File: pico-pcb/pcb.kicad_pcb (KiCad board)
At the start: 2 copper layers, 53.3 x 71.1 mm, 28 parts, among them J1 AudioJack1, J2 AudioJack2, Q1 2N3904, SW1 SW_DIP_x04, U1 Pico

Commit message: Updated PCB .50mm traces now and rewired trrs jack to match digirig type cabling.
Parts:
-  : renamed from REF** (x2)
- 3.2mm M3: renamed from REF** (x2)
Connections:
- J1 pad R1: SP -> MIC
- J1 pad T: MIC -> SP
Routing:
- net GND: track 204.5 -> 199.8 mm
- net PTT_R: track 146.2 -> 143.3 mm
- net MIC: track 16.0 -> 17.7 mm
- net SP: track 11.9 -> 11.0 mm

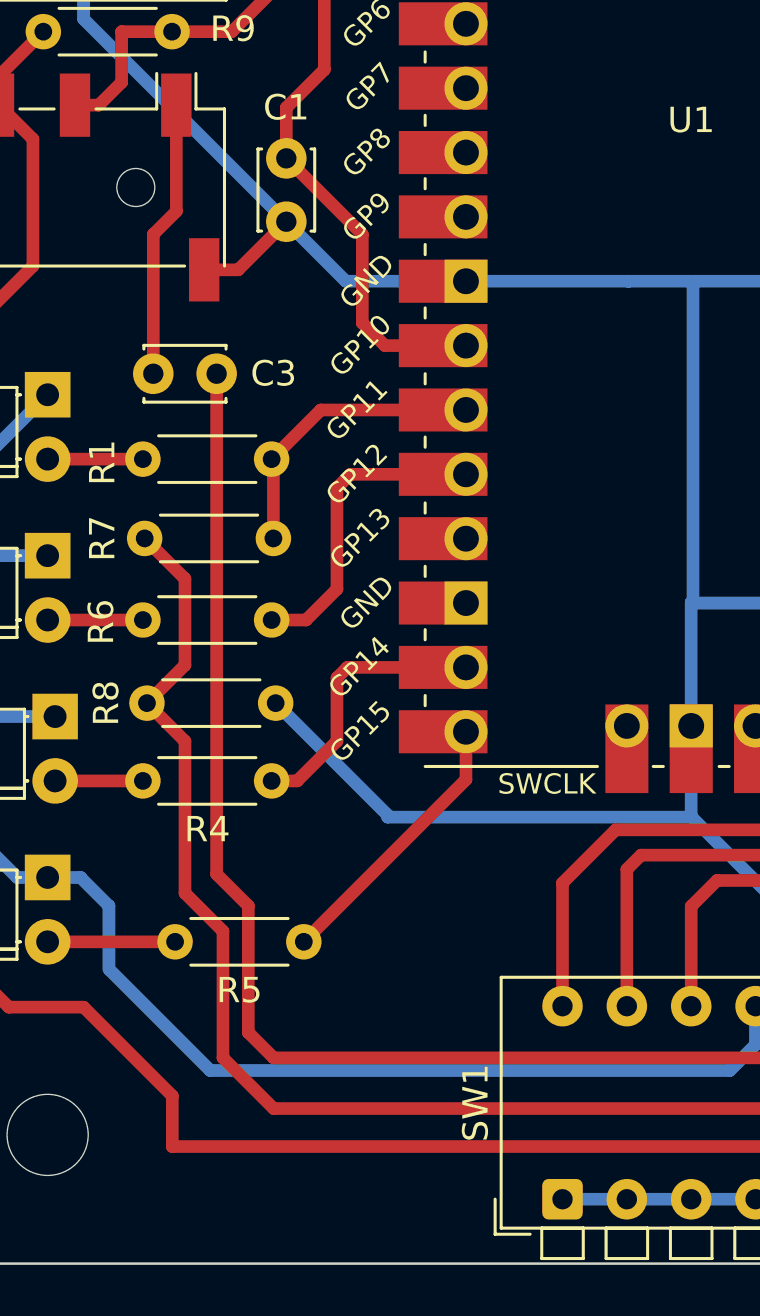
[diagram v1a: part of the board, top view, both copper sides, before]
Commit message: Updated Schematic and PCB to add 100ohm resistor to pwm circuit as per original pico tnc and recommendation by Mario AE0GL
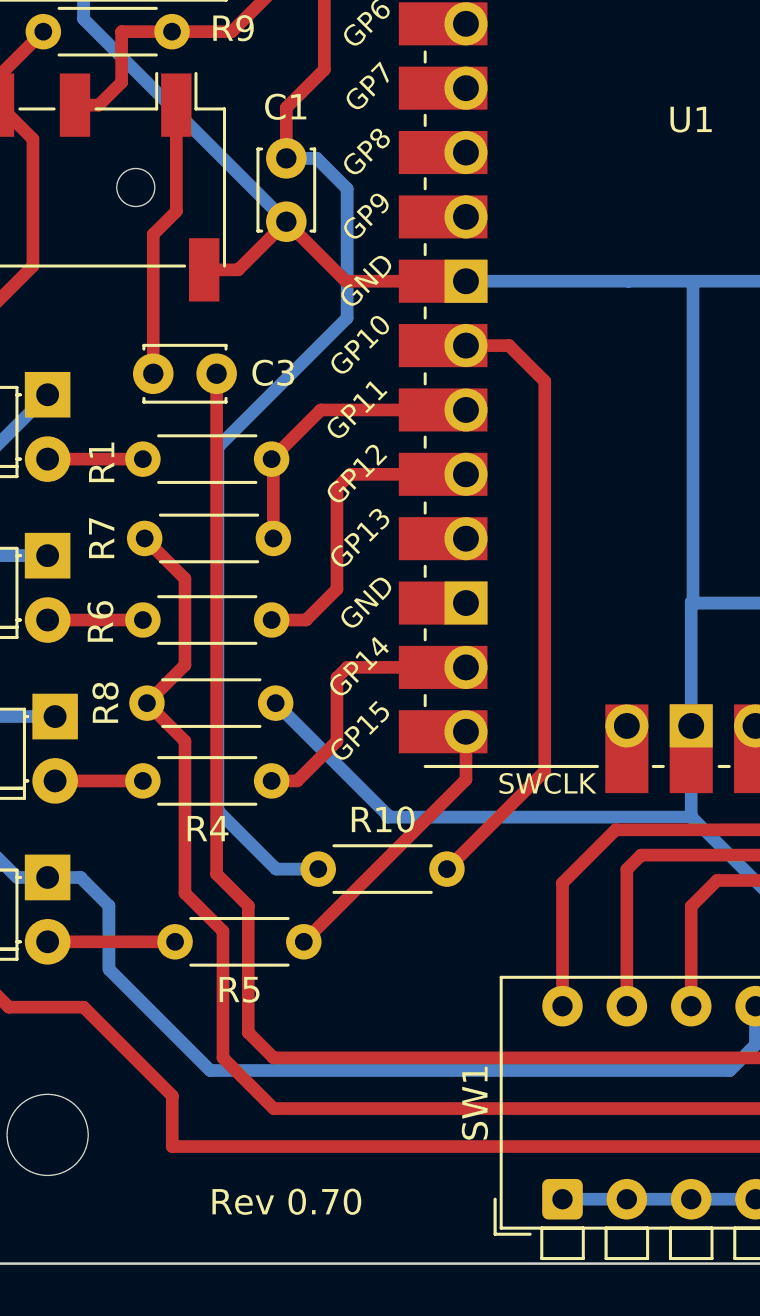
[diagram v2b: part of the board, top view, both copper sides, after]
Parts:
- added R10: 100, Resistor_THT:R_Axial_DIN0204_L3.6mm_D1.6mm_P5.08mm_Horizontal, F.Cu at (87.9, 105.5)
- C1, C2: value 100n -> 100nF
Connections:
- net PSAVE renamed OPT2
- C1 pad 1: PWM -> Net-(C1-Pad1)
- RV1 pad 1: PWM -> Net-(C1-Pad1)
- SW1 pad 6: OPT1 -> OPT3
- SW1 pad 8: KISS -> OPT1
- U1 pad 21: KISS -> OPT1
- U1 pad 24: OPT1 -> OPT3
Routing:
- net Net-(C1-Pad1): track 0.00 -> 63.5 mm
- net OPT3: track 0.00 -> 35.8 mm
- net KISS: track 22.5 -> 0.00 mm
- net PWM: track 41.2 -> 24.5 mm
- net OPT1: track 35.8 -> 22.5 mm
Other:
- board text added: "Rev 0.70"
